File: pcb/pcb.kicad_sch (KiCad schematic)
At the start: 0 parts

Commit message: feat: added pcb files
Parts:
- added A_REG_1_8, A_REG_9_16: SN74HC574N, 74hc:20pdip, symbol 74hc:SN74HC574N
- added A_REG_BUS_1_8, A_REG_BUS_9_16: SN74HC245N, 74hc:20pdip, symbol 74hc:SN74HC245N
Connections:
- new net: A_REG_1_8.12 (8Q), A_REG_BUS_1_8.9 (A8)
- new net: A_REG_1_8.13 (7Q), A_REG_BUS_1_8.8 (A7)
- new net: A_REG_1_8.14 (6Q), A_REG_BUS_1_8.7 (A6)
- new net: A_REG_1_8.15 (5Q), A_REG_BUS_1_8.6 (A5)
- new net: A_REG_1_8.16 (4Q), A_REG_BUS_1_8.5 (A4)
- new net: A_REG_1_8.17 (3Q), A_REG_BUS_1_8.4 (A3)
- new net: A_REG_1_8.18 (2Q), A_REG_BUS_1_8.3 (A2)
- new net: A_REG_1_8.19 (1Q), A_REG_BUS_1_8.2 (A1)
- new net: A_REG_9_16.12 (8Q), A_REG_BUS_9_16.9 (A8)
- new net: A_REG_9_16.13 (7Q), A_REG_BUS_9_16.8 (A7)
- new net: A_REG_9_16.14 (6Q), A_REG_BUS_9_16.7 (A6)
- new net: A_REG_9_16.15 (5Q), A_REG_BUS_9_16.6 (A5)
- new net: A_REG_9_16.16 (4Q), A_REG_BUS_9_16.5 (A4)
- new net: A_REG_9_16.17 (3Q), A_REG_BUS_9_16.4 (A3)
- new net: A_REG_9_16.18 (2Q), A_REG_BUS_9_16.3 (A2)
- new net: A_REG_9_16.19 (1Q), A_REG_BUS_9_16.2 (A1)
- new net +5V: A_REG_1_8.20 (VCC), A_REG_9_16.20 (VCC), A_REG_BUS_1_8.1 (DIR), A_REG_BUS_1_8.20 (VCC), A_REG_BUS_9_16.1 (DIR), A_REG_BUS_9_16.20 (VCC)
- new net A_REG_1_8_CLK: A_REG_1_8.11 (CLK)
- new net A_REG_9_16_CLK: A_REG_9_16.11 (CLK)
- new net DB_1: A_REG_1_8.9 (8D)
- new net DB_10: A_REG_9_16.8 (7D)
- new net DB_11: A_REG_9_16.7 (6D)
- new net DB_12: A_REG_9_16.6 (5D)
- new net DB_13: A_REG_9_16.5 (4D)
- new net DB_14: A_REG_9_16.4 (3D)
- new net DB_15: A_REG_9_16.3 (2D)
- new net DB_16: A_REG_9_16.2 (1D)
- new net DB_2: A_REG_1_8.8 (7D)
- new net DB_3: A_REG_1_8.7 (6D)
- new net DB_4: A_REG_1_8.6 (5D)
- new net DB_5: A_REG_1_8.5 (4D)
- new net DB_6: A_REG_1_8.4 (3D)
- new net DB_7: A_REG_1_8.3 (2D)
- new net DB_8: A_REG_1_8.2 (1D)
- new net DB_9: A_REG_9_16.9 (8D)
- new net GND: A_REG_1_8.1 (*OE), A_REG_1_8.10 (GND), A_REG_9_16.1 (*OE), A_REG_9_16.10 (GND), A_REG_BUS_1_8.10 (GND), A_REG_BUS_9_16.10 (GND)

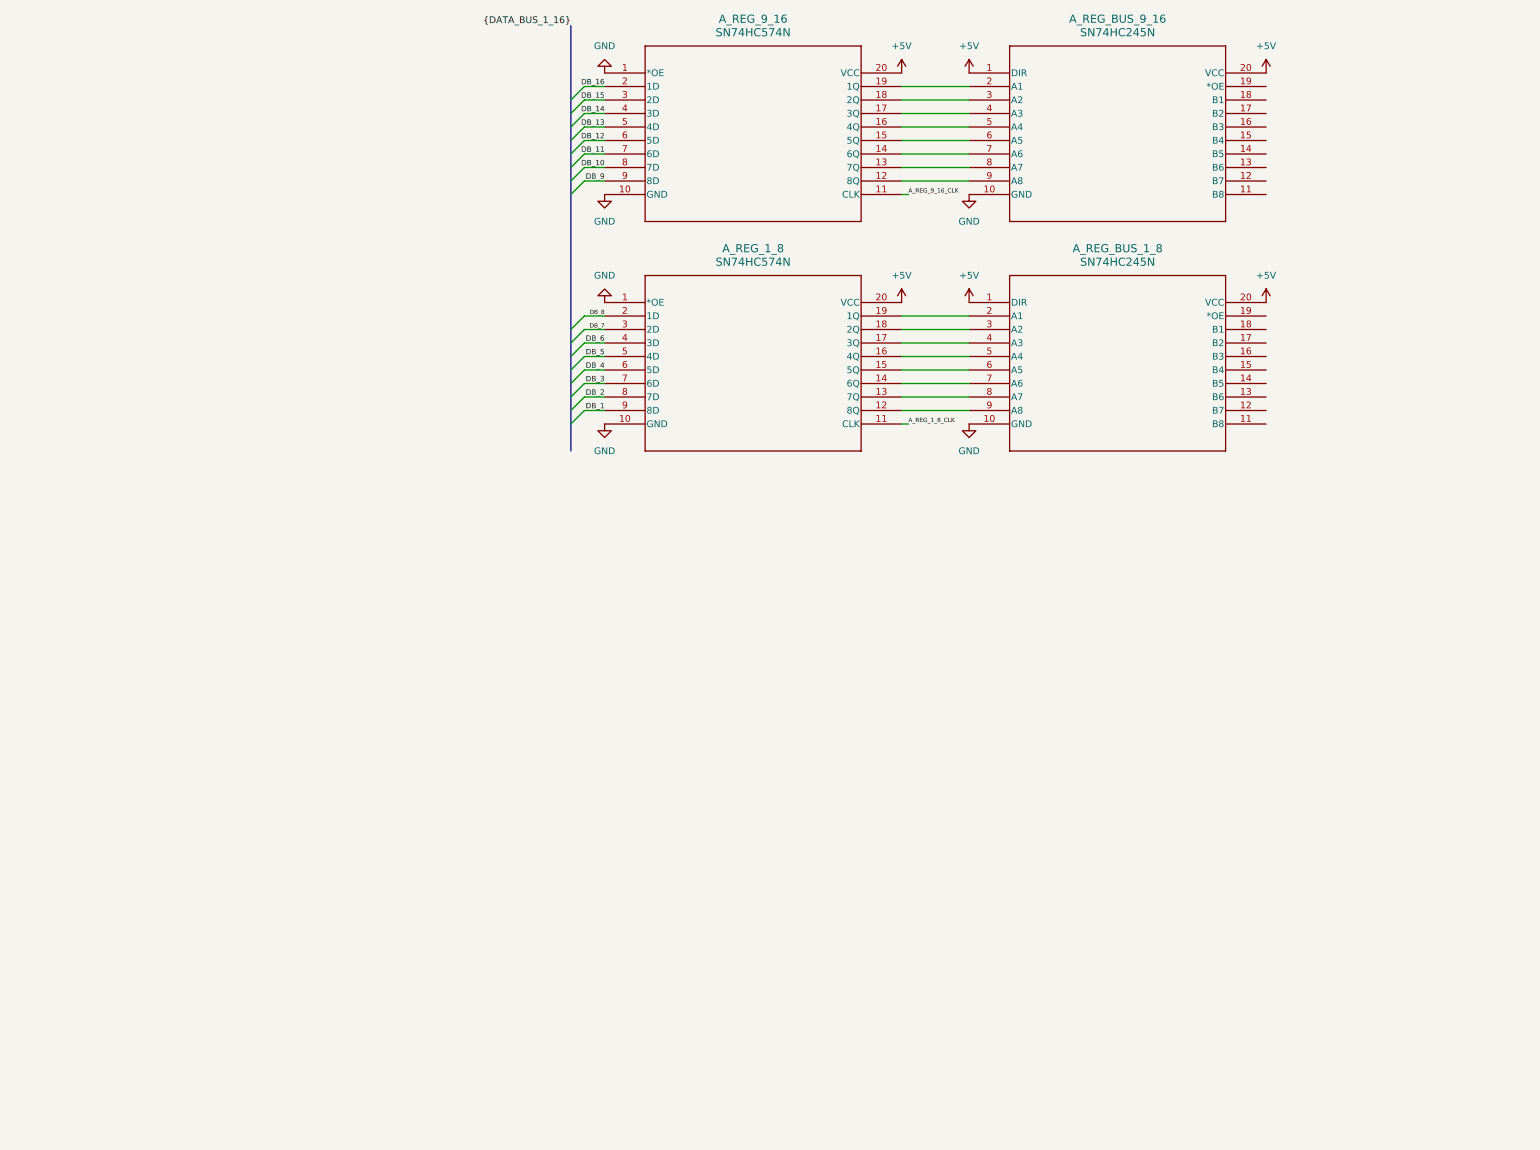
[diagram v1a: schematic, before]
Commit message: feat: low bits of register a and b pcb design done
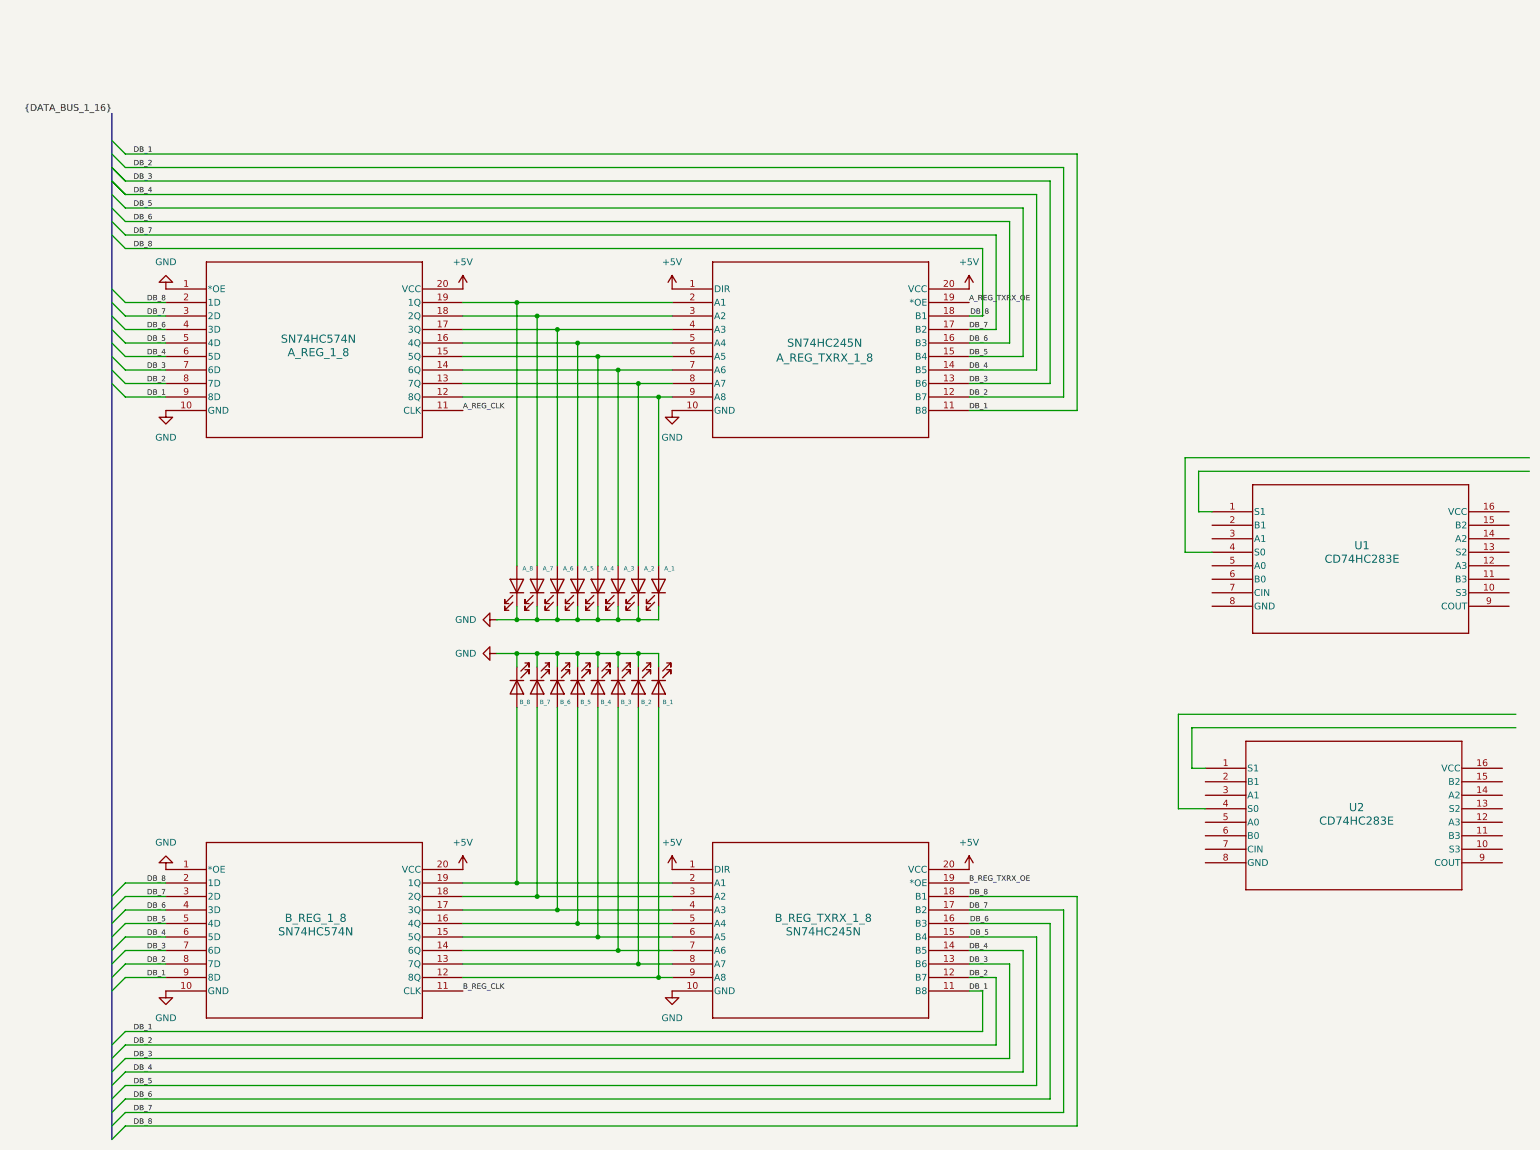
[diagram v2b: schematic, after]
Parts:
- removed A_REG_BUS_1_8: SN74HC245N, 74hc:20pdip, symbol 74hc:SN74HC245N
- added A_1, A_2, A_3, A_4, A_5, A_6, A_7, A_8, B_1, B_2, B_3, B_4, B_5, B_6, B_7, B_8: LED, symbol Device:LED
- added A_REG_TXRX_1_8: SN74HC245N, 74hc:20pdip, symbol 74hc:SN74HC245N
- added U1, U2: CD74HC283E, 74hc:16pdip, symbol 74hc:CD74HC283E
- renumbered A_REG_9_16 to B_REG_1_8, A_REG_BUS_9_16 to B_REG_TXRX_1_8
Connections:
- net DB_10 is gone; now on net DB_2: B_REG_1_8.8 (7D)
- net DB_11 is gone; now on net DB_3: B_REG_1_8.7 (6D)
- net DB_12 is gone; now on net DB_4: B_REG_1_8.6 (5D)
- net DB_13 is gone; now on net DB_5: B_REG_1_8.5 (4D)
- net DB_14 is gone; now on net DB_6: B_REG_1_8.4 (3D)
- net DB_15 is gone; now on net DB_7: B_REG_1_8.3 (2D)
- net DB_16 is gone; now on net DB_8: B_REG_1_8.2 (1D)
- net DB_9 is gone; now on net DB_1: B_REG_1_8.9 (8D)
- net +5V: now also A_REG_TXRX_1_8.1 (DIR), A_REG_TXRX_1_8.20 (VCC)
- net DB_1: now also B_REG_TXRX_1_8.11 (B8), A_REG_TXRX_1_8.11 (B8)
- net DB_2: now also B_REG_TXRX_1_8.12 (B7), A_REG_TXRX_1_8.12 (B7)
- net DB_3: now also B_REG_TXRX_1_8.13 (B6), A_REG_TXRX_1_8.13 (B6)
- net DB_4: now also B_REG_TXRX_1_8.14 (B5), A_REG_TXRX_1_8.14 (B5)
- net DB_5: now also B_REG_TXRX_1_8.15 (B4), A_REG_TXRX_1_8.15 (B4)
- net DB_6: now also B_REG_TXRX_1_8.16 (B3), A_REG_TXRX_1_8.16 (B3)
- net DB_7: now also B_REG_TXRX_1_8.17 (B2), A_REG_TXRX_1_8.17 (B2)
- net DB_8: now also B_REG_TXRX_1_8.18 (B1), A_REG_TXRX_1_8.18 (B1)
- net GND: now also A_1.1 (K), A_2.1 (K), A_3.1 (K), A_4.1 (K), A_5.1 (K), A_6.1 (K), A_7.1 (K), A_8.1 (K), A_REG_TXRX_1_8.10 (GND), B_1.1 (K), B_2.1 (K), B_3.1 (K), B_4.1 (K), B_5.1 (K), B_6.1 (K), B_7.1 (K), B_8.1 (K)
- net at A_REG_1_8.12 (8Q): now also A_1.2 (A), A_REG_TXRX_1_8.9 (A8)
- net at A_REG_1_8.13 (7Q): now also A_2.2 (A), A_REG_TXRX_1_8.8 (A7)
- net at A_REG_1_8.14 (6Q): now also A_3.2 (A), A_REG_TXRX_1_8.7 (A6)
- net at A_REG_1_8.15 (5Q): now also A_4.2 (A), A_REG_TXRX_1_8.6 (A5)
- net at A_REG_1_8.16 (4Q): now also A_5.2 (A), A_REG_TXRX_1_8.5 (A4)
- net at A_REG_1_8.17 (3Q): now also A_6.2 (A), A_REG_TXRX_1_8.4 (A3)
- net at A_REG_1_8.18 (2Q): now also A_7.2 (A), A_REG_TXRX_1_8.3 (A2)
- net at A_REG_1_8.19 (1Q): now also A_8.2 (A), A_REG_TXRX_1_8.2 (A1)
- net at B_REG_1_8.12 (8Q), B_REG_TXRX_1_8.9 (A8): now also B_1.2 (A)
- net at B_REG_1_8.13 (7Q), B_REG_TXRX_1_8.8 (A7): now also B_2.2 (A)
- net at B_REG_1_8.14 (6Q), B_REG_TXRX_1_8.7 (A6): now also B_3.2 (A)
- net at B_REG_1_8.15 (5Q), B_REG_TXRX_1_8.6 (A5): now also B_4.2 (A)
- net at B_REG_1_8.16 (4Q), B_REG_TXRX_1_8.5 (A4): now also B_5.2 (A)
- net at B_REG_1_8.17 (3Q), B_REG_TXRX_1_8.4 (A3): now also B_6.2 (A)
- net at B_REG_1_8.18 (2Q), B_REG_TXRX_1_8.3 (A2): now also B_7.2 (A)
- net at B_REG_1_8.19 (1Q), B_REG_TXRX_1_8.2 (A1): now also B_8.2 (A)
- net B_REG_TXRX_OE: now reaches B_REG_TXRX_1_8.19 (*OE)
- net A_REG_1_8_CLK renamed A_REG_CLK
- net A_REG_9_16_CLK renamed B_REG_CLK
- new net A_REG_TXRX_OE: A_REG_TXRX_1_8.19 (*OE)
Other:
- moved on the sheet: B_REG_1_8, B_REG_TXRX_1_8

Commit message: feat: pcb routed for 16 bit a register
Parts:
- added B_1, B_10, B_11, B_12, B_13, B_14, B_15, B_16, B_2, B_3, B_4, B_5, B_6, B_7, B_8, B_9: LED, LED_THT:LED_D5.0mm, symbol Device:LED
- added B_REG_1_9, B_REG_9_17: SN74HC574N, 74hc:20pdip, symbol 74hc:SN74HC574N
- added B_REG_TXRX_1_9, B_REG_TXRX_9_17: SN74HC245N, 74hc:20pdip, symbol 74hc:SN74HC245N
- added NAND_1_4, NAND_5_8: SN74HC00N, 74hc:14pdip, symbol 74hc:SN74HC00N
- A_1, A_2, A_3, A_5, A_6, A_7, A_8: footprint (none) -> LED_THT:LED_D5.0mm
- A_10: renamed from B_2; footprint (none) -> LED_THT:LED_D5.0mm
- A_11: renamed from B_3; footprint (none) -> LED_THT:LED_D5.0mm
- A_12: renamed from B_4; footprint (none) -> LED_THT:LED_D5.0mm
- A_13: renamed from B_5; footprint (none) -> LED_THT:LED_D5.0mm
- A_14: renamed from B_6; footprint (none) -> LED_THT:LED_D5.0mm
- A_15: renamed from B_7; footprint (none) -> LED_THT:LED_D5.0mm
- A_16: renamed from B_8; footprint (none) -> LED_THT:LED_D5.0mm
- A_9: renamed from B_1; footprint (none) -> LED_THT:LED_D5.0mm
- renumbered B_REG_1_8 to A_REG_9_16, B_REG_TXRX_1_8 to A_REG_TXRX_9_16, U1 to FULL_ADDER_1_4, U2 to FULL_ADDER_5_8
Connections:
- net +5V: now also FULL_ADDER_1_4.16 (VCC), FULL_ADDER_5_8.16 (VCC), B_REG_1_9.20 (VCC), B_REG_9_17.20 (VCC), B_REG_TXRX_1_9.1 (DIR), B_REG_TXRX_1_9.20 (VCC), B_REG_TXRX_9_17.1 (DIR), B_REG_TXRX_9_17.20 (VCC), NAND_1_4.14 (VCC), NAND_5_8.14 (VCC)
- net A_REG_CLK: now also A_REG_9_16.11 (CLK)
- net A_REG_TXRX_OE: now also A_REG_TXRX_9_16.19 (*OE)
- net B_REG_CLK: now also B_REG_1_9.11 (CLK), B_REG_9_17.11 (CLK); no longer A_REG_9_16.11 (CLK)
- net B_REG_TXRX_OE: now also B_REG_TXRX_1_9.19 (*OE), B_REG_TXRX_9_17.19 (*OE); no longer A_REG_TXRX_9_16.19 (*OE)
- net DB_1: now also B_REG_1_9.9 (8D), B_REG_TXRX_1_9.11 (B8); no longer A_REG_9_16.9 (8D), A_REG_TXRX_9_16.11 (B8)
- net DB_2: now also B_REG_1_9.8 (7D), B_REG_TXRX_1_9.12 (B7); no longer A_REG_9_16.8 (7D), A_REG_TXRX_9_16.12 (B7)
- net DB_3: now also B_REG_1_9.7 (6D), B_REG_TXRX_1_9.13 (B6); no longer A_REG_9_16.7 (6D), A_REG_TXRX_9_16.13 (B6)
- net DB_4: now also B_REG_1_9.6 (5D), B_REG_TXRX_1_9.14 (B5); no longer A_REG_9_16.6 (5D), A_REG_TXRX_9_16.14 (B5)
- net DB_5: now also B_REG_1_9.5 (4D), B_REG_TXRX_1_9.15 (B4); no longer A_REG_9_16.5 (4D), A_REG_TXRX_9_16.15 (B4)
- net DB_6: now also B_REG_1_9.4 (3D), B_REG_TXRX_1_9.16 (B3); no longer A_REG_9_16.4 (3D), A_REG_TXRX_9_16.16 (B3)
- net DB_7: now also B_REG_1_9.3 (2D), B_REG_TXRX_1_9.17 (B2); no longer A_REG_9_16.3 (2D), A_REG_TXRX_9_16.17 (B2)
- net DB_8: now also B_REG_1_9.2 (1D), B_REG_TXRX_1_9.18 (B1); no longer A_REG_9_16.2 (1D), A_REG_TXRX_9_16.18 (B1)
- net GND: now also FULL_ADDER_1_4.8 (GND), FULL_ADDER_5_8.8 (GND), B_1.1 (K), B_10.1 (K), B_11.1 (K), B_12.1 (K), B_13.1 (K), B_14.1 (K), B_15.1 (K), B_16.1 (K), B_2.1 (K), B_3.1 (K), B_4.1 (K), B_5.1 (K), B_6.1 (K), B_7.1 (K), B_8.1 (K), B_9.1 (K), B_REG_1_9.1 (*OE), B_REG_1_9.10 (GND), B_REG_9_17.1 (*OE), B_REG_9_17.10 (GND), B_REG_TXRX_1_9.10 (GND), B_REG_TXRX_9_17.10 (GND), NAND_1_4.7 (GND), NAND_5_8.7 (GND)
- net B_8: now reaches FULL_ADDER_5_8.11 (B3)
- net B_8: now also B_8.2 (A), B_REG_1_9.19 (1Q), B_REG_TXRX_1_9.2 (A1), NAND_5_8.13 (4B)
- net A_8: now reaches FULL_ADDER_5_8.12 (A3)
- net A_8: now also A_8.2 (A), A_REG_1_8.19 (1Q), A_REG_TXRX_1_8.2 (A1), NAND_5_8.12 (4A)
- net A_7: now reaches FULL_ADDER_5_8.14 (A2)
- net A_7: now also A_7.2 (A), A_REG_1_8.18 (2Q), A_REG_TXRX_1_8.3 (A2), NAND_5_8.9 (3A)
- net B_7: now reaches FULL_ADDER_5_8.15 (B2)
- net B_7: now also B_7.2 (A), B_REG_1_9.18 (2Q), B_REG_TXRX_1_9.3 (A2), NAND_5_8.10 (3B)
- net B_6: now reaches FULL_ADDER_5_8.2 (B1)
- net B_6: now also B_6.2 (A), B_REG_1_9.17 (3Q), B_REG_TXRX_1_9.4 (A3), NAND_5_8.5 (2B)
- net A_6: now reaches FULL_ADDER_5_8.3 (A1)
- net A_6: now also A_6.2 (A), A_REG_1_8.17 (3Q), A_REG_TXRX_1_8.4 (A3), NAND_5_8.4 (2A)
- net A_5: now reaches FULL_ADDER_5_8.5 (A0)
- net A_5: now also A_5.2 (A), A_REG_1_8.16 (4Q), A_REG_TXRX_1_8.5 (A4), NAND_5_8.1 (1A)
- net B_5: now reaches FULL_ADDER_5_8.6 (B0)
- net B_5: now also B_5.2 (A), B_REG_1_9.16 (4Q), B_REG_TXRX_1_9.5 (A4), NAND_5_8.2 (1B)
- net at FULL_ADDER_5_8.7 (CIN): now also FULL_ADDER_1_4.9 (COUT)
- net A_12: now reaches A_12.2 (A), A_REG_9_16.15 (5Q), A_REG_TXRX_9_16.6 (A5)
- net A_3: now reaches A_3.2 (A), A_REG_1_8.14 (6Q), A_REG_TXRX_1_8.7 (A6)
- net A_3: now also FULL_ADDER_1_4.14 (A2), NAND_1_4.9 (3A)
- net A_13: now reaches A_13.2 (A), A_REG_9_16.16 (4Q), A_REG_TXRX_9_16.5 (A4)
- net A_4: now reaches A_4.2 (A), A_REG_1_8.15 (5Q), A_REG_TXRX_1_8.6 (A5)
- net A_4: now also FULL_ADDER_1_4.12 (A3), NAND_1_4.12 (4A)
- net A_2: now reaches A_2.2 (A), A_REG_1_8.13 (7Q), A_REG_TXRX_1_8.8 (A7)
- net A_2: now also FULL_ADDER_1_4.3 (A1), NAND_1_4.4 (2A)
- net A_1: now reaches A_1.2 (A), A_REG_1_8.12 (8Q), A_REG_TXRX_1_8.9 (A8)
- net A_1: now also FULL_ADDER_1_4.5 (A0), NAND_1_4.1 (1A)
- net A_15: now reaches A_15.2 (A), A_REG_9_16.18 (2Q), A_REG_TXRX_9_16.3 (A2)
- net A_11: now reaches A_11.2 (A), A_REG_9_16.14 (6Q), A_REG_TXRX_9_16.7 (A6)
- net A_14: now reaches A_14.2 (A), A_REG_9_16.17 (3Q), A_REG_TXRX_9_16.4 (A3)
- net A_9: now reaches A_9.2 (A), A_REG_9_16.12 (8Q), A_REG_TXRX_9_16.9 (A8)
- net A_10: now reaches A_10.2 (A), A_REG_9_16.13 (7Q), A_REG_TXRX_9_16.8 (A7)
- net A_16: now reaches A_16.2 (A), A_REG_9_16.19 (1Q), A_REG_TXRX_9_16.2 (A1)
- net B_4: now reaches FULL_ADDER_1_4.11 (B3)
- net B_4: now also B_4.2 (A), B_REG_1_9.15 (5Q), B_REG_TXRX_1_9.6 (A5), NAND_1_4.13 (4B)
- net B_3: now reaches FULL_ADDER_1_4.15 (B2)
- net B_3: now also B_3.2 (A), B_REG_1_9.14 (6Q), B_REG_TXRX_1_9.7 (A6), NAND_1_4.10 (3B)
- net B_2: now reaches FULL_ADDER_1_4.2 (B1)
- net B_2: now also B_2.2 (A), B_REG_1_9.13 (7Q), B_REG_TXRX_1_9.8 (A7), NAND_1_4.5 (2B)
- net B_1: now reaches FULL_ADDER_1_4.6 (B0)
- net B_1: now also B_1.2 (A), B_REG_1_9.12 (8Q), B_REG_TXRX_1_9.9 (A8), NAND_1_4.2 (1B)
- new net B_10: B_10.2 (A), B_REG_9_17.13 (7Q), B_REG_TXRX_9_17.8 (A7)
- new net B_11: B_11.2 (A), B_REG_9_17.14 (6Q), B_REG_TXRX_9_17.7 (A6)
- new net B_12: B_12.2 (A), B_REG_9_17.15 (5Q), B_REG_TXRX_9_17.6 (A5)
- new net B_13: B_13.2 (A), B_REG_9_17.16 (4Q), B_REG_TXRX_9_17.5 (A4)
- new net B_14: B_14.2 (A), B_REG_9_17.17 (3Q), B_REG_TXRX_9_17.4 (A3)
- new net B_15: B_15.2 (A), B_REG_9_17.18 (2Q), B_REG_TXRX_9_17.3 (A2)
- new net B_16: B_16.2 (A), B_REG_9_17.19 (1Q), B_REG_TXRX_9_17.2 (A1)
- new net B_9: B_9.2 (A), B_REG_9_17.12 (8Q), B_REG_TXRX_9_17.9 (A8)
- new net DB_10: A_REG_9_16.8 (7D), A_REG_TXRX_9_16.12 (B7), B_REG_9_17.8 (7D), B_REG_TXRX_9_17.12 (B7)
- new net DB_11: A_REG_9_16.7 (6D), A_REG_TXRX_9_16.13 (B6), B_REG_9_17.7 (6D), B_REG_TXRX_9_17.13 (B6)
- new net DB_12: A_REG_9_16.6 (5D), A_REG_TXRX_9_16.14 (B5), B_REG_9_17.6 (5D), B_REG_TXRX_9_17.14 (B5)
- new net DB_13: A_REG_9_16.5 (4D), A_REG_TXRX_9_16.15 (B4), B_REG_9_17.5 (4D), B_REG_TXRX_9_17.15 (B4)
- new net DB_14: A_REG_9_16.4 (3D), A_REG_TXRX_9_16.16 (B3), B_REG_9_17.4 (3D), B_REG_TXRX_9_17.16 (B3)
- new net DB_15: A_REG_9_16.3 (2D), A_REG_TXRX_9_16.17 (B2), B_REG_9_17.3 (2D), B_REG_TXRX_9_17.17 (B2)
- new net DB_16: A_REG_9_16.2 (1D), A_REG_TXRX_9_16.18 (B1), B_REG_9_17.2 (1D), B_REG_TXRX_9_17.18 (B1)
- new net DB_9: A_REG_9_16.9 (8D), A_REG_TXRX_9_16.11 (B8), B_REG_9_17.9 (8D), B_REG_TXRX_9_17.11 (B8)
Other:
- moved on the sheet: FULL_ADDER_1_4, FULL_ADDER_5_8

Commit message: feat: schematic for full adder mostly done
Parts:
- added FULL_ADDER_13_16, FULL_ADDER_9_12: CD74HC283E, 74hc:16pdip, symbol 74hc:CD74HC283E
- added FULL_ADDER_TXRX_1_8, FULL_ADDER_TXRX_9_16: SN74HC245N, 74hc:20pdip, symbol 74hc:SN74HC245N
- added NAND_13_16, NAND_9_12: SN74HC00N, 74hc:14pdip, symbol 74hc:SN74HC00N
- A_4: footprint (none) -> LED_THT:LED_D5.0mm
- renumbered B_REG_1_9 to B_REG_1_8, B_REG_9_17 to B_REG_9_16, B_REG_TXRX_1_9 to B_REG_TXRX_1_8, B_REG_TXRX_9_17 to B_REG_TXRX_9_16
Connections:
- net +5V: now also FULL_ADDER_13_16.16 (VCC), FULL_ADDER_9_12.16 (VCC), FULL_ADDER_TXRX_1_8.1 (DIR), FULL_ADDER_TXRX_1_8.20 (VCC), FULL_ADDER_TXRX_9_16.1 (DIR), FULL_ADDER_TXRX_9_16.20 (VCC), NAND_13_16.14 (VCC), NAND_9_12.14 (VCC)
- net A_10: now also FULL_ADDER_9_12.3 (A1), NAND_9_12.4 (2A)
- net A_11: now also FULL_ADDER_9_12.14 (A2), NAND_9_12.10 (3B)
- net A_12: now also FULL_ADDER_9_12.12 (A3), NAND_9_12.12 (4A)
- net A_13: now also FULL_ADDER_13_16.5 (A0), NAND_13_16.1 (1A)
- net A_14: now also FULL_ADDER_13_16.3 (A1), NAND_13_16.4 (2A)
- net A_15: now also FULL_ADDER_13_16.14 (A2), NAND_13_16.10 (3B)
- net A_16: now also FULL_ADDER_13_16.12 (A3), NAND_13_16.12 (4A)
- net A_3: now also NAND_1_4.10 (3B); no longer NAND_1_4.9 (3A)
- net A_7: now also NAND_5_8.10 (3B); no longer NAND_5_8.9 (3A)
- net A_9: now also FULL_ADDER_9_12.5 (A0), NAND_9_12.1 (1A)
- net B_10: now also FULL_ADDER_9_12.2 (B1), NAND_9_12.5 (2B)
- net B_11: now also FULL_ADDER_9_12.15 (B2), NAND_9_12.9 (3A)
- net B_12: now also FULL_ADDER_9_12.11 (B3), NAND_9_12.13 (4B)
- net B_13: now also FULL_ADDER_13_16.6 (B0), NAND_13_16.2 (1B)
- net B_14: now also FULL_ADDER_13_16.2 (B1), NAND_13_16.5 (2B)
- net B_15: now also FULL_ADDER_13_16.15 (B2), NAND_13_16.9 (3A)
- net B_16: now also FULL_ADDER_13_16.11 (B3), NAND_13_16.13 (4B)
- net B_3: now also NAND_1_4.9 (3A); no longer NAND_1_4.10 (3B)
- net B_7: now also NAND_5_8.9 (3A); no longer NAND_5_8.10 (3B)
- net B_9: now also FULL_ADDER_9_12.6 (B0), NAND_9_12.2 (1B)
- net GND: now also FULL_ADDER_13_16.8 (GND), FULL_ADDER_9_12.8 (GND), FULL_ADDER_TXRX_1_8.10 (GND), FULL_ADDER_TXRX_9_16.10 (GND), NAND_13_16.7 (GND), NAND_9_12.7 (GND)
- net AR_6: now reaches FULL_ADDER_5_8.1 (S1)
- net AR_6: now also FULL_ADDER_TXRX_1_8.7 (A6)
- net AR_8: now reaches FULL_ADDER_5_8.10 (S3)
- net AR_8: now also FULL_ADDER_TXRX_1_8.9 (A8)
- net AR_7: now reaches FULL_ADDER_5_8.13 (S2)
- net AR_7: now also FULL_ADDER_TXRX_1_8.8 (A7)
- net AR_5: now reaches FULL_ADDER_5_8.4 (S0)
- net AR_5: now also FULL_ADDER_TXRX_1_8.6 (A5)
- net at FULL_ADDER_5_8.9 (COUT): now also FULL_ADDER_9_12.7 (CIN)
- net NND_4: now reaches NAND_1_4.11 (4Y)
- net NND_1: now reaches NAND_1_4.3 (1Y)
- net NND_2: now reaches NAND_1_4.6 (2Y)
- net NND_3: now reaches NAND_1_4.8 (3Y)
- net NND_8: now reaches NAND_5_8.11 (4Y)
- net NND_5: now reaches NAND_5_8.3 (1Y)
- net NND_6: now reaches NAND_5_8.6 (2Y)
- net NND_7: now reaches NAND_5_8.8 (3Y)
- net AR_2: now reaches FULL_ADDER_1_4.1 (S1)
- net AR_2: now also FULL_ADDER_TXRX_1_8.3 (A2)
- net AR_4: now reaches FULL_ADDER_1_4.10 (S3)
- net AR_4: now also FULL_ADDER_TXRX_1_8.5 (A4)
- net AR_3: now reaches FULL_ADDER_1_4.13 (S2)
- net AR_3: now also FULL_ADDER_TXRX_1_8.4 (A3)
- net AR_1: now reaches FULL_ADDER_1_4.4 (S0)
- net AR_1: now also FULL_ADDER_TXRX_1_8.2 (A1)
- new net: FULL_ADDER_13_16.7 (CIN), FULL_ADDER_9_12.9 (COUT)
- new net AR_10: FULL_ADDER_9_12.1 (S1), FULL_ADDER_TXRX_9_16.3 (A2)
- new net AR_11: FULL_ADDER_9_12.13 (S2), FULL_ADDER_TXRX_9_16.4 (A3)
- new net AR_12: FULL_ADDER_9_12.10 (S3), FULL_ADDER_TXRX_9_16.5 (A4)
- new net AR_13: FULL_ADDER_13_16.4 (S0), FULL_ADDER_TXRX_9_16.6 (A5)
- new net AR_14: FULL_ADDER_13_16.1 (S1), FULL_ADDER_TXRX_9_16.7 (A6)
- new net AR_15: FULL_ADDER_13_16.13 (S2), FULL_ADDER_TXRX_9_16.8 (A7)
- new net AR_16: FULL_ADDER_13_16.10 (S3), FULL_ADDER_TXRX_9_16.9 (A8)
- new net AR_9: FULL_ADDER_9_12.4 (S0), FULL_ADDER_TXRX_9_16.2 (A1)
- new net NND_10: NAND_9_12.6 (2Y)
- new net NND_11: NAND_9_12.8 (3Y)
- new net NND_12: NAND_9_12.11 (4Y)
- new net NND_13: NAND_13_16.3 (1Y)
- new net NND_14: NAND_13_16.6 (2Y)
- new net NND_15: NAND_13_16.8 (3Y)
- new net NND_16: NAND_13_16.11 (4Y)
- new net NND_9: NAND_9_12.3 (1Y)
